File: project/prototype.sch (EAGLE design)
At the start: 0 parts

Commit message: Add components
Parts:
- added U$1, U$5, U$9: RJ12, components:RJ12
- added U$10, U$11, U$2, U$3, U$6, U$7: CPC1017N, components:CPC1017N
- added U$12, U$4, U$8: NX7002AK, components:NX7002AK
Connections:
- new net N$1: U$1.C1-H, U$2.LOAD@2
- new net N$10: U$11.LOAD@1, U$5.C2-L, U$7.LOAD@2, U$9.C1-L
- new net N$11: U$6.+, U$7.+
- new net N$12: U$6.-, U$7.-
- new net N$15: U$10.LOAD@1, U$9.C2-H
- new net N$16: U$11.LOAD@2, U$9.C2-L
- new net N$17: U$10.+, U$11.+
- new net N$18: U$10.-, U$11.-
- new net N$2: U$1.C1-L, U$3.LOAD@1
- new net N$3: U$1.C2-H, U$2.LOAD@1, U$5.C1-H, U$6.LOAD@2
- new net N$4: U$1.C2-L, U$3.LOAD@2, U$5.C1-L, U$7.LOAD@1
- new net N$5: U$2.+, U$3.+
- new net N$7: U$2.-, U$3.-
- new net N$9: U$10.LOAD@2, U$5.C2-H, U$6.LOAD@1, U$9.C1-H

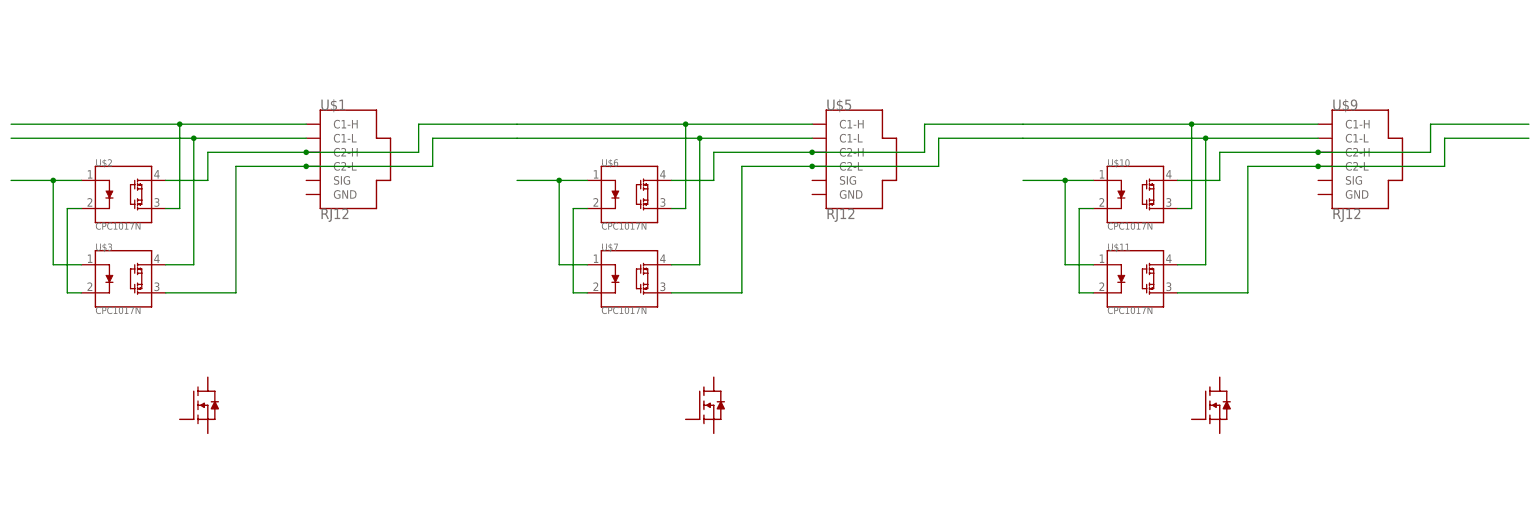
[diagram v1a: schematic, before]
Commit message: Add red LED
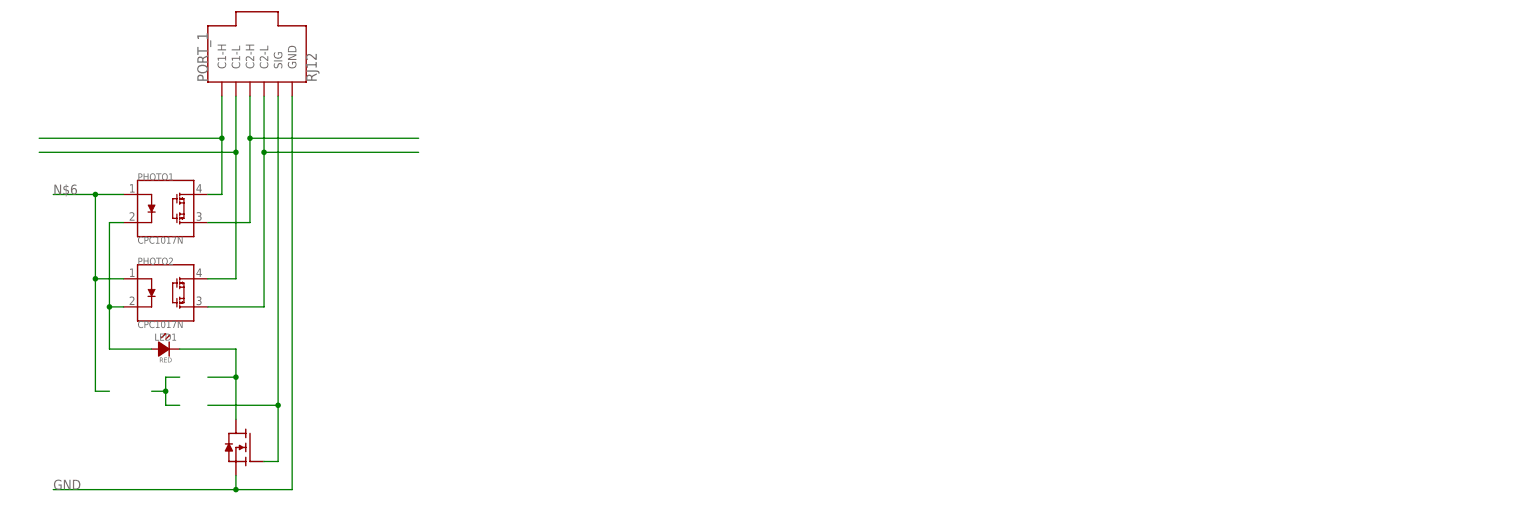
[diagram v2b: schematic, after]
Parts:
- removed U$1, U$5, U$9: RJ12, components:RJ12
- removed U$10, U$11, U$2, U$3, U$6, U$7: CPC1017N, components:CPC1017N
- removed U$12, U$4, U$8: NX7002AK, components:NX7002AK
- added LED1: RED, components:150060RS75000
- added MOSFET1: NX7002AK, components:NX7002AK
- added PHOTO1, PHOTO2: CPC1017N, components:CPC1017N
- added PORT_1: RJ12, components:RJ12
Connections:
- removed net N$10: U$11.LOAD@1, U$5.C2-L, U$7.LOAD@2, U$9.C1-L
- removed net N$11: U$6.+, U$7.+
- removed net N$12: U$6.-, U$7.-
- removed net N$15: U$10.LOAD@1, U$9.C2-H
- removed net N$16: U$11.LOAD@2, U$9.C2-L
- removed net N$17: U$10.+, U$11.+
- removed net N$18: U$10.-, U$11.-
- removed net N$9: U$10.LOAD@2, U$5.C2-H, U$6.LOAD@1, U$9.C1-H
- new net GND: MOSFET1.SOURCE, PORT_1.GND
- new net N$6: PHOTO1.+, PHOTO2.+
- new net N$8: LED1.-, MOSFET1.DRAIN
- net N$1: now also PHOTO1.LOAD@1, PORT_1.C1-H; no longer U$1.C1-H, U$2.LOAD@2
- net N$2: now also PHOTO1.LOAD@2, PORT_1.C2-H; no longer U$1.C1-L, U$3.LOAD@1
- net N$3: now also PHOTO2.LOAD@1, PORT_1.C1-L; no longer U$1.C2-H, U$2.LOAD@1, U$5.C1-H, U$6.LOAD@2
- net N$4: now also PHOTO2.LOAD@2, PORT_1.C2-L; no longer U$1.C2-L, U$3.LOAD@2, U$5.C1-L, U$7.LOAD@1
- net N$5: now also MOSFET1.GATE, PORT_1.SIG; no longer U$2.+, U$3.+
- net N$7: now also LED1.+, PHOTO1.-, PHOTO2.-; no longer U$2.-, U$3.-

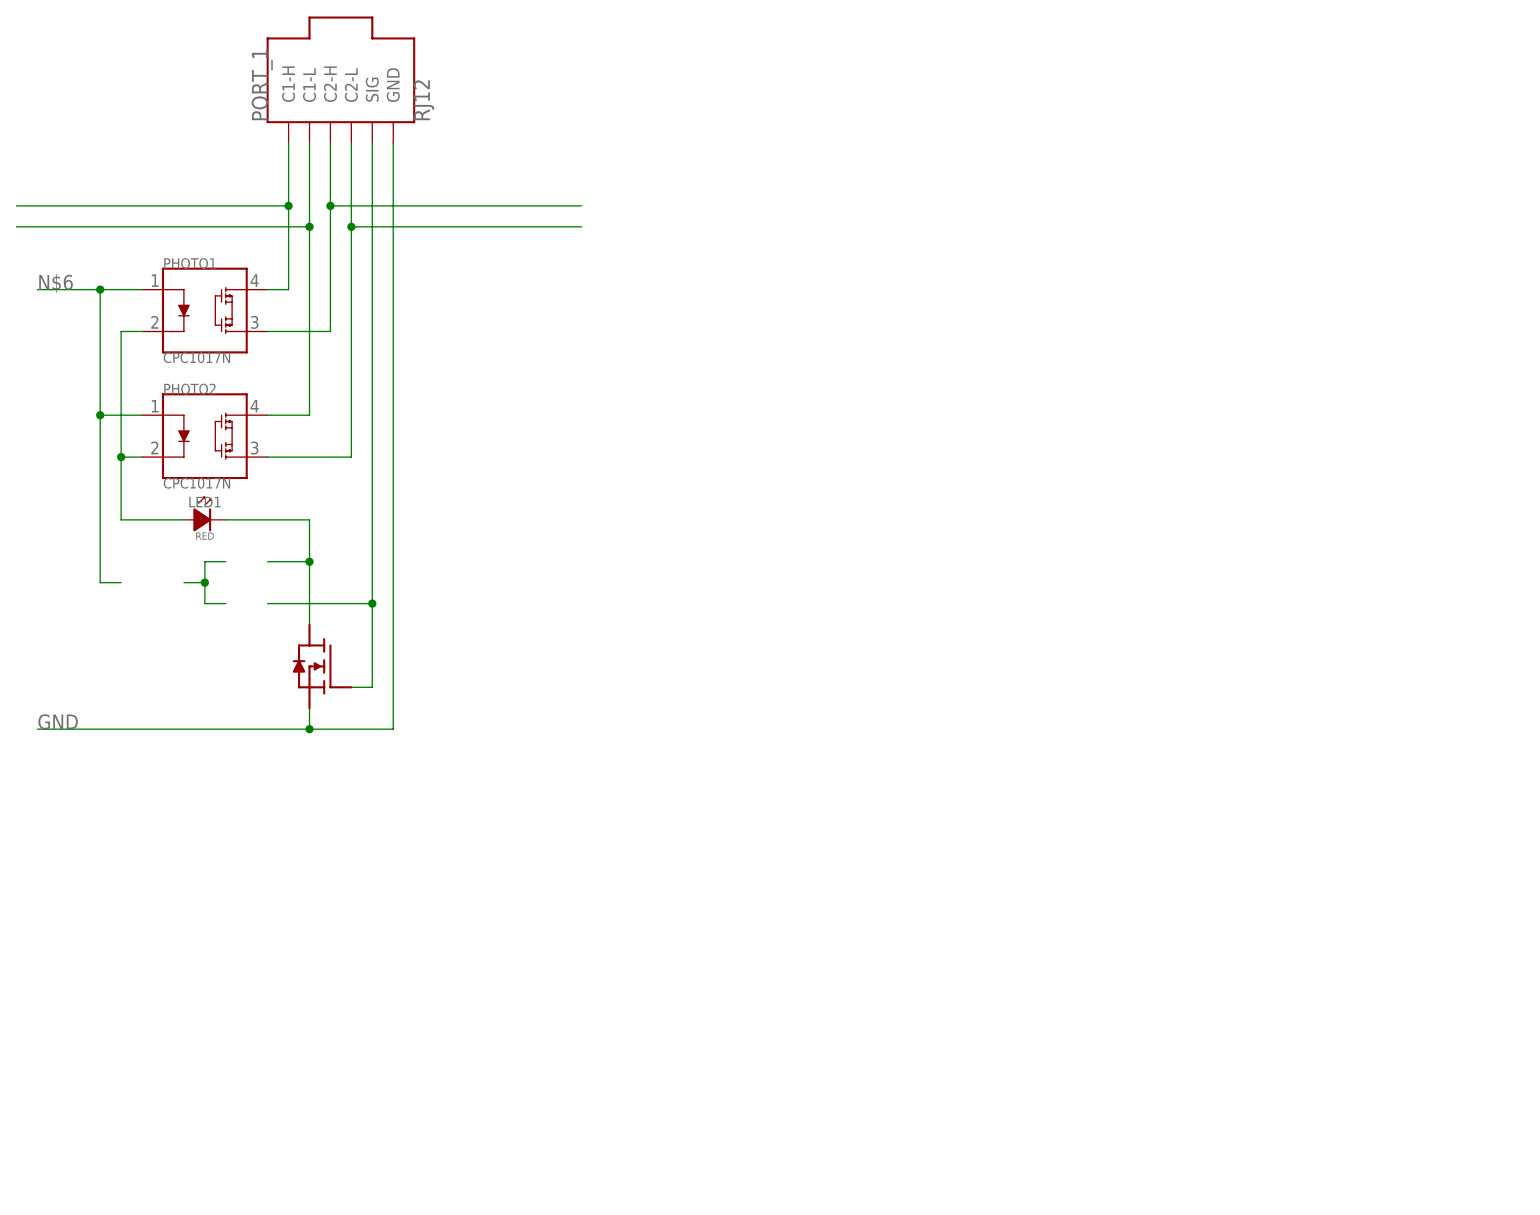
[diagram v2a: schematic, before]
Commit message: Add indicator schematic
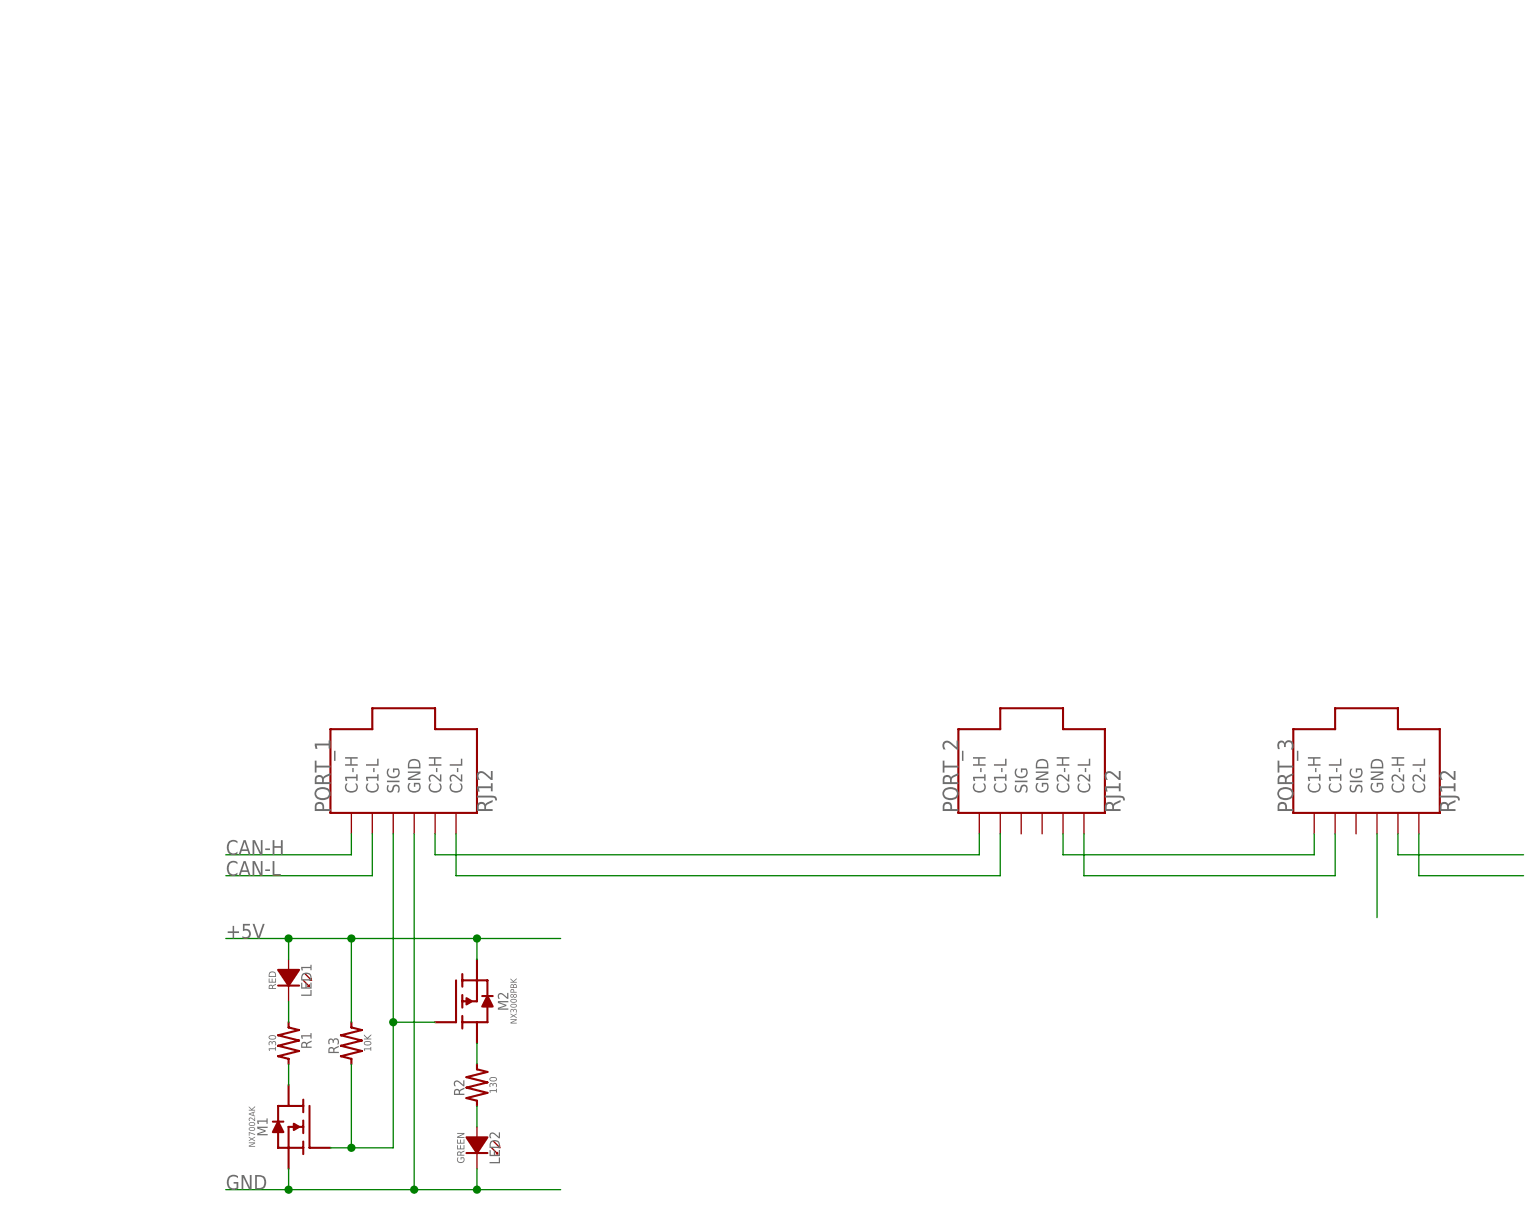
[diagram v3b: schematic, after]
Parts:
- removed MOSFET1: NX7002AK, components:NX7002AK
- removed PHOTO1, PHOTO2: CPC1017N, components:CPC1017N
- added LED2: GREEN, components:150060VS75000
- added M1: NX7002AK, components:NX7002AK
- added M2: NX3008PBK, components:NX3008PBK
- added PORT_2, PORT_3: RJ12, components:RJ12
- added R1, R2: 130, components:1300402
- added R3: 10K, components:10K0402
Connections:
- new net +5V: LED1.+, M2.SOURCE, R3.2
- new net CAN-H: PORT_1.C1-H
- new net CAN-L: PORT_1.C1-L
- new net GATE: M1.GATE, M2.GATE, PORT_1.SIG, R3.1
- new net N$10: LED2.+, R2.1
- new net N$9: PORT_3.C2-L
- net GND: now also LED2.-, M1.SOURCE, PORT_3.GND; no longer MOSFET1.SOURCE
- net N$1: now also LED1.-, R1.1; no longer PHOTO1.LOAD@1, PORT_1.C1-H
- net N$2: now also M1.DRAIN, R1.2; no longer PHOTO1.LOAD@2, PORT_1.C2-H
- net N$3: now also PORT_1.C2-H, PORT_2.C1-H; no longer PHOTO2.LOAD@1, PORT_1.C1-L
- net N$4: now also M2.DRAIN, R2.2; no longer PHOTO2.LOAD@2, PORT_1.C2-L
- net N$5: now also PORT_3.C2-H; no longer MOSFET1.GATE, PORT_1.SIG
- net N$6: now also PORT_1.C2-L, PORT_2.C1-L; no longer PHOTO1.+, PHOTO2.+
- net N$7: now also PORT_2.C2-H, PORT_3.C1-H; no longer LED1.+, PHOTO1.-, PHOTO2.-
- net N$8: now also PORT_2.C2-L, PORT_3.C1-L; no longer LED1.-, MOSFET1.DRAIN
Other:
- moved on the sheet: LED1, PORT_1

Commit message: Add input terminal blocks
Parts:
- removed PORT_1, PORT_2, PORT_3: RJ12, components:RJ12
- added LED10, LED12, LED16, LED20, LED24, LED3, LED6, LED8: GREEN, components:150060VS75000
- added LED11, LED15, LED19, LED23, LED5, LED7, LED9: RED, components:150060RS75000
- added M10, M12, M16, M20, M24, M6, M8: NX7002AK, components:NX7002AK
- added M11, M15, M19, M23, M5, M7, M9: NX3008PBK, components:NX3008PBK
- added P1, P2, P3, P4, P5, P6, P7, P8: RJ12, components:RJ12
- added R10, R13, R16, R22, R28, R34, R7: 10K, components:10K0402
- added R11, R12, R14, R15, R17, R18, R23, R24, R29, R30, R35, R36, R4, R8, R9: 130, components:1300402
- added U$1: TERMINAL_BLOCK, components:TERMINAL_BLOCK
- added U$2: POWER_BLOCK, components:POWER_BLOCK
- M1: value NX7002AK -> NX3008PBK; device components:NX7002AK -> components:NX3008PBK
- M2: value NX3008PBK -> NX7002AK; device components:NX3008PBK -> components:NX7002AK
- R1: value 130 -> 10K; device components:1300402 -> components:10K0402
- R3: value 10K -> 130; device components:10K0402 -> components:1300402
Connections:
- removed net CAN-H: PORT_1.C1-H
- removed net CAN-L: PORT_1.C1-L
- removed net GATE: M1.GATE, M2.GATE, PORT_1.SIG, R3.1
- removed net N$10: LED2.+, R2.1
- removed net N$2: M1.DRAIN, R1.2
- removed net N$3: PORT_1.C2-H, PORT_2.C1-H
- removed net N$5: PORT_3.C2-H
- removed net N$6: PORT_1.C2-L, PORT_2.C1-L
- removed net N$7: PORT_2.C2-H, PORT_3.C1-H
- new net CAN_IN_H: P1.C1-H, U$1.1
- new net CAN_IN_L: P1.C1-L, U$1.2
- new net CAN_OUT_H: P8.C2-H, U$1.3
- new net CAN_OUT_L: P8.C2-L, U$1.4
- new net GATE1: M1.GATE, M2.GATE, P1.SIG, R1.1
- new net GATE11: M23.GATE, M24.GATE, P8.SIG, R34.1
- new net GATE2: M5.GATE, M6.GATE, P2.SIG, R7.1
- new net GATE3: M7.GATE, M8.GATE, P3.SIG, R10.1
- new net GATE4: M10.GATE, M9.GATE, P4.SIG, R13.1
- new net GATE5: M11.GATE, M12.GATE, P5.SIG, R16.1
- new net GATE7: M15.GATE, M16.GATE, P6.SIG, R22.1
- new net GATE9: M19.GATE, M20.GATE, P7.SIG, R28.1
- new net N$11: LED1.-, R2.1
- new net N$15: P1.C2-H, P2.C1-H
- new net N$16: M7.DRAIN, R12.2
- new net N$17: M5.DRAIN, R9.2
- new net N$18: LED6.+, R9.1
- new net N$19: LED5.-, R8.1
- new net N$20: M6.DRAIN, R8.2
- new net N$21: LED8.+, R12.1
- new net N$22: P1.C2-L, P2.C1-L
- new net N$23: P2.C2-H, P3.C1-H
- new net N$24: P2.C2-L, P3.C1-L
- new net N$25: LED7.-, R11.1
- new net N$26: M8.DRAIN, R11.2
- new net N$27: M11.DRAIN, R18.2
- new net N$28: LED12.+, R18.1
- new net N$29: P3.C2-H, P4.C1-H
- new net N$30: P3.C2-L, P4.C1-L
- new net N$31: M9.DRAIN, R15.2
- new net N$32: LED10.+, R15.1
- new net N$33: LED9.-, R14.1
- new net N$34: M10.DRAIN, R14.2
- new net N$35: LED11.-, R17.1
- new net N$36: M12.DRAIN, R17.2
- new net N$37: P4.C2-H, P5.C1-H
- new net N$38: P4.C2-L, P5.C1-L
- new net N$51: M15.DRAIN, R24.2
- new net N$52: LED16.+, R24.1
- new net N$53: LED15.-, R23.1
- new net N$54: M16.DRAIN, R23.2
- new net N$55: P5.C2-H, P6.C1-H
- new net N$56: P5.C2-L, P6.C1-L
- new net N$67: M19.DRAIN, R30.2
- new net N$68: LED20.+, R30.1
- new net N$69: LED19.-, R29.1
- new net N$70: M20.DRAIN, R29.2
- new net N$71: P6.C2-H, P7.C1-H
- new net N$72: P6.C2-L, P7.C1-L
- new net N$83: M23.DRAIN, R36.2
- new net N$84: LED24.+, R36.1
- new net N$85: LED23.-, R35.1
- new net N$86: M24.DRAIN, R35.2
- new net N$87: P7.C2-H, P8.C1-H
- new net N$88: P7.C2-L, P8.C1-L
- net +5V: now also LED11.+, LED15.+, LED19.+, LED23.+, LED5.+, LED7.+, LED9.+, M1.SOURCE, M11.SOURCE, M15.SOURCE, M19.SOURCE, M23.SOURCE, M5.SOURCE, M7.SOURCE, M9.SOURCE, R1.2, R10.2, R13.2, R16.2, R22.2, R28.2, R34.2, R4.2, R7.2, U$2.1; no longer M2.SOURCE, R3.2
- net GND: now also LED10.-, LED12.-, LED16.-, LED20.-, LED24.-, LED3.-, LED6.-, LED8.-, M10.SOURCE, M12.SOURCE, M16.SOURCE, M2.SOURCE, M20.SOURCE, M24.SOURCE, M6.SOURCE, M8.SOURCE, P1.GND, P2.GND, P3.GND, P4.GND, P5.GND, P6.GND, P7.GND, P8.GND, U$2.2; no longer M1.SOURCE, PORT_1.GND, PORT_3.GND
- net N$1: now also LED3.+, R4.1; no longer LED1.-, R1.1
- net N$8: now also M1.DRAIN, R3.2; no longer PORT_2.C2-L, PORT_3.C1-L
- net N$9: now also LED2.+, R3.1; no longer PORT_3.C2-L
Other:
- moved on the sheet: LED1, LED2, M1, M2, R1, R2, R3
